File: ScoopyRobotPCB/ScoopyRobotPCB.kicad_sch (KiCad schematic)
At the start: 19 parts, among them J2 18V battery, J3 Raspberry_Pi_Header, M1 Gearmotor with encoder, M2 Gearmotor with encoder, M3 Roller gearmotor, M4 Tray gearmotor, SW1 Roller position, SW2 Tray down, SW3 Tray up, SW4 Pushbutton, SW5 Emergency stop, U1 D24V25F5 voltage regulator mo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

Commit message: Fixed typos in labels, connected properly now
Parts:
- renumbered J2 to J1, J3 to J2, M3 to M1, M4 to M2, M1 to M3, M2 to M4, U1 to Mod1, Mod1 to Mod2, Mod2 to Mod3, SW4 to SW1, SW5 to SW2, SW1 to SW3, SW2 to SW4, SW3 to SW5
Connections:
- net Roller position is gone; now on net Roll position: SW3.2 (B)
- net GND: now also J2.34 (Ground), J2.9 (Ground)
- net UI.SW: now also SW1.3 (B), SW1.4 (B)
- no-connect marks 7 -> 8
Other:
- moved on the sheet: SW1

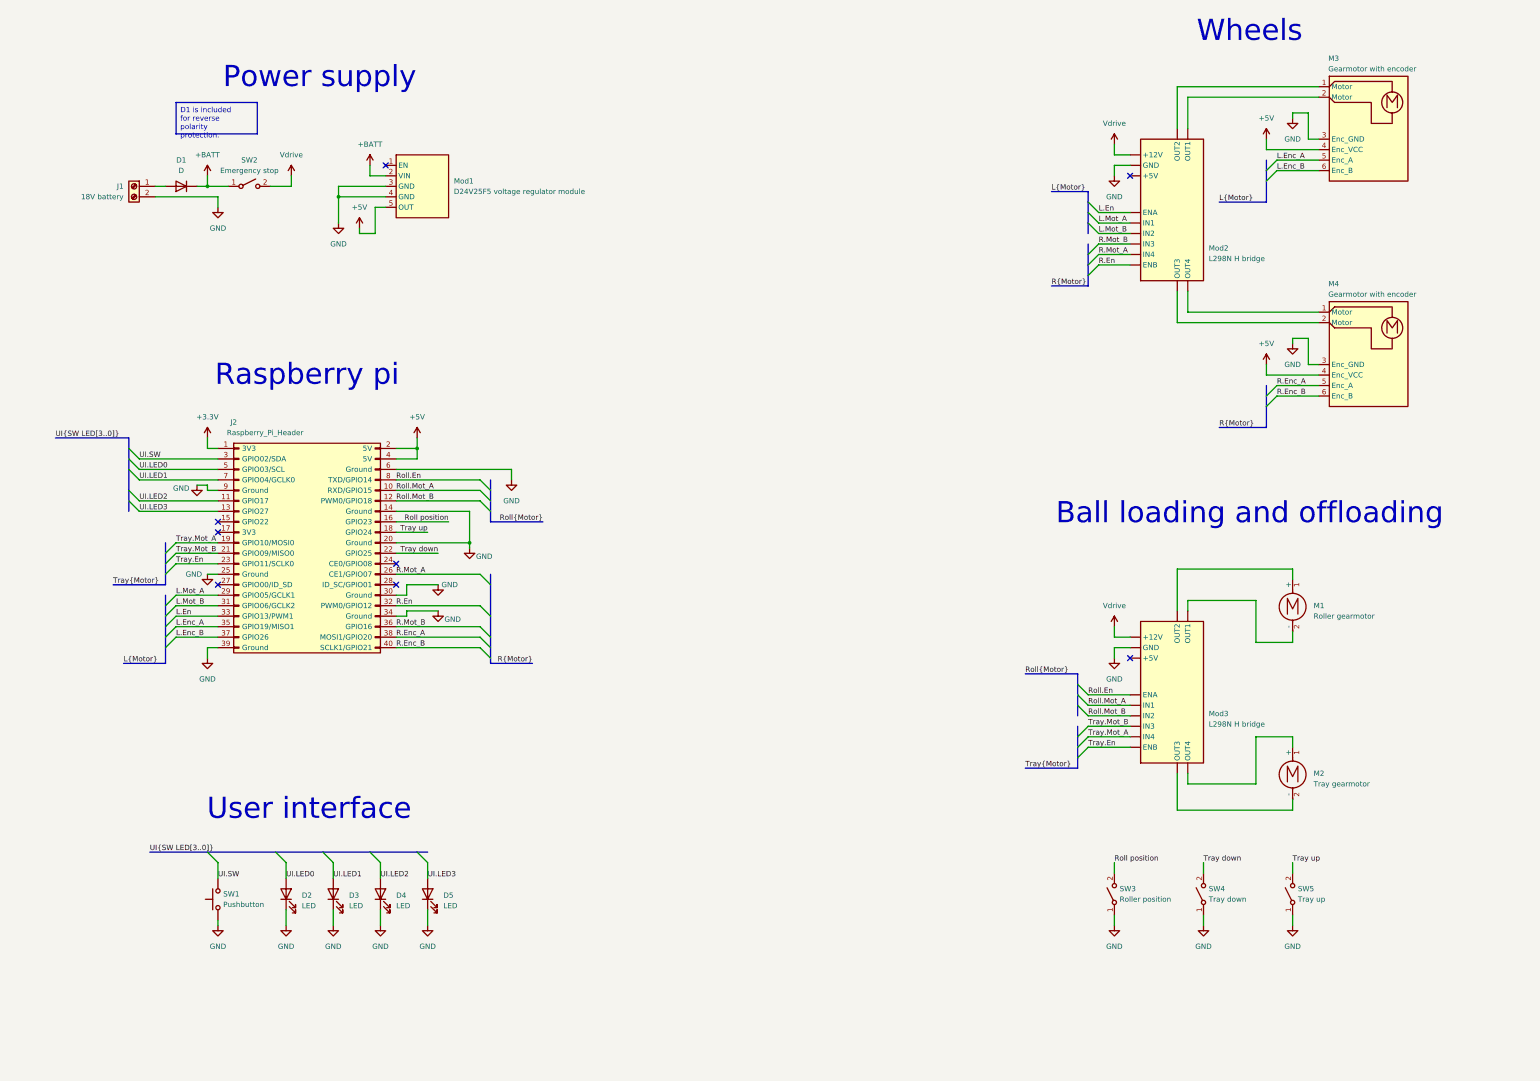
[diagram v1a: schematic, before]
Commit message: Fixing mistakes and typos in schematic, assigning footprints, starting veroboard layout
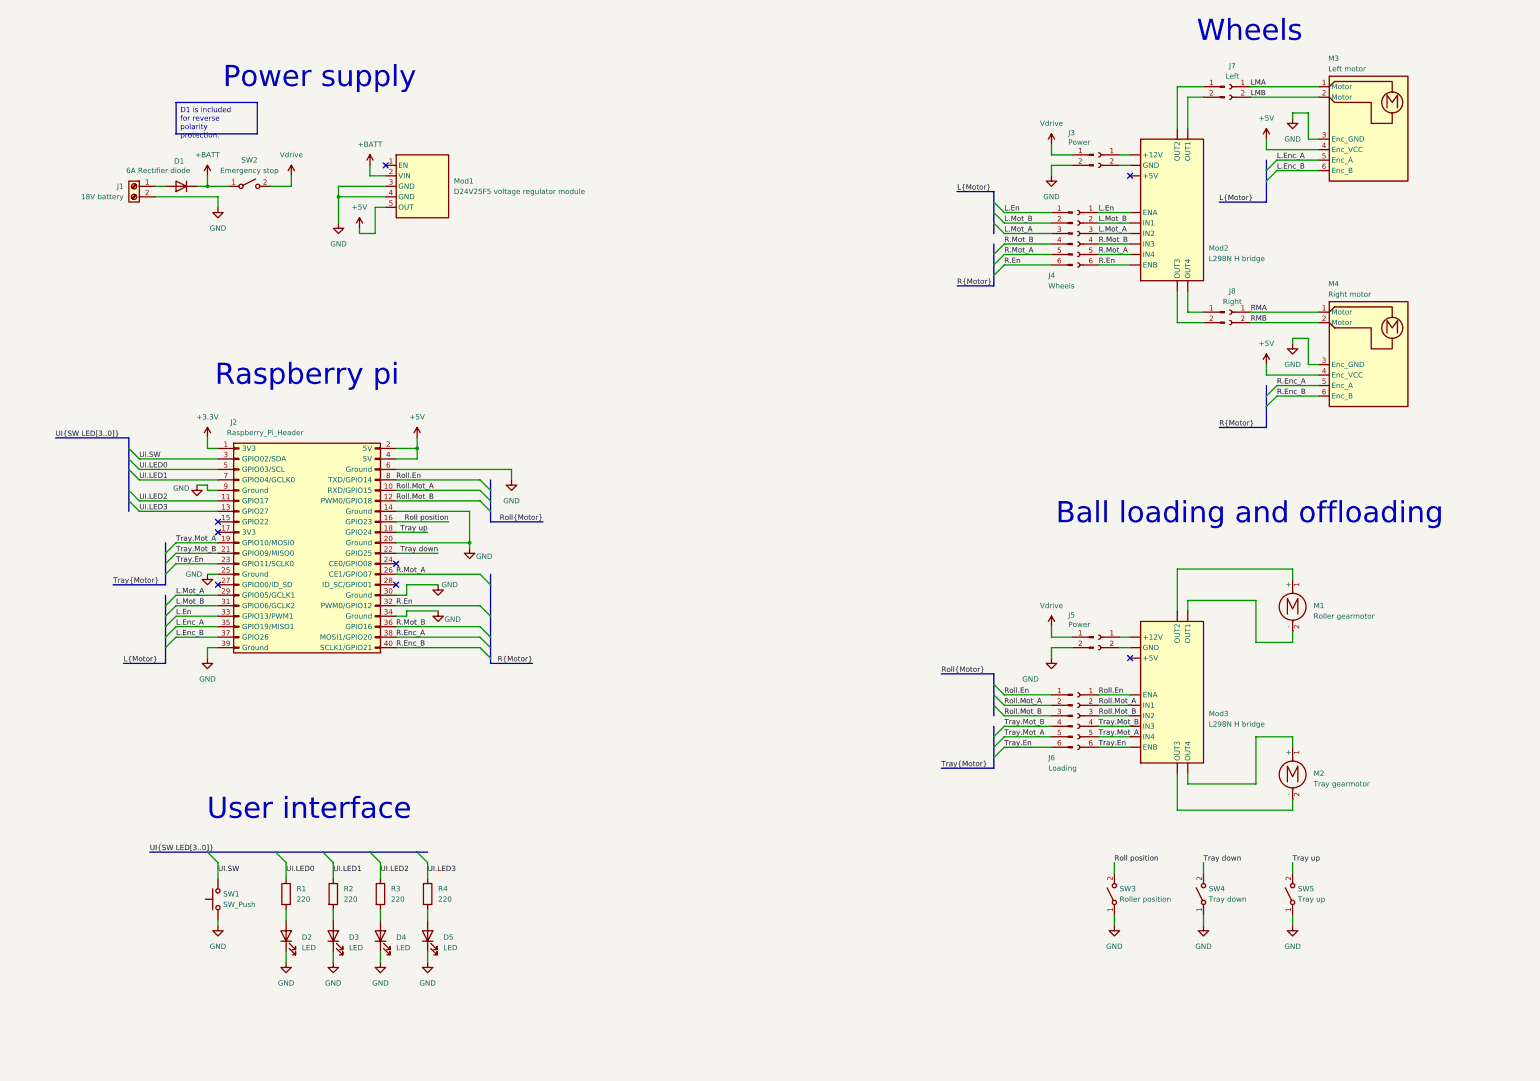
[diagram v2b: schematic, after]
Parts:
- removed SW1: Pushbutton, symbol Switch:SW_MEC_5G
- added #1, #3: Conn_01x02_Socket, symbol Connector:Conn_01x02_Socket
- added #2, #4: Wheels, symbol Connector:Conn_01x06_Socket
- added #5: Left motor, Connector_PinHeader_2.54mm:PinHeader_1x02_P2.54mm_Vertical, symbol Connector:Conn_01x02_Pin
- added #6: Right motor, Connector_PinHeader_2.54mm:PinHeader_1x02_P2.54mm_Vertical, symbol Connector:Conn_01x02_Pin
- added J3, J5: Power, Connector_PinHeader_2.54mm:PinHeader_1x02_P2.54mm_Vertical, symbol Connector:Conn_01x02_Pin
- added J4: Wheels, Connector_PinHeader_2.54mm:PinHeader_1x06_P2.54mm_Vertical, symbol Connector:Conn_01x06_Pin
- added J6: Loading, Connector_PinHeader_2.54mm:PinHeader_1x06_P2.54mm_Vertical, symbol Connector:Conn_01x06_Pin
- added J7: Left, Connector_PinSocket_2.54mm:PinSocket_1x02_P2.54mm_Vertical, symbol Connector:Conn_01x02_Socket
- added J8: Right, Connector_PinSocket_2.54mm:PinSocket_1x02_P2.54mm_Vertical, symbol Connector:Conn_01x02_Socket
- added R1, R2, R3, R4: 220, Resistor_THT:R_Axial_DIN0411_L9.9mm_D3.6mm_P12.70mm_Horizontal, symbol Device:R
- added SW1: SW_Push, Button_Switch_SMD:SW_SPST_Omron_B3FS-100xP, symbol Switch:SW_Push
- D1: value D -> 6A Rectifier diode; footprint (none) -> Diode_THT:D_DO-201_P15.24mm_Horizontal
- D2, D3, D4, D5: footprint (none) -> LED_THT:LED_D5.0mm
- J1, M1, M2, SW2: footprint (none) -> TerminalBlock_Phoenix:TerminalBlock_Phoenix_MKDS-1,5-2_1x02_P5.00mm_Horizontal
- M3: value Gearmotor with encoder -> Left motor; footprint (none) -> Connector_PinHeader_2.54mm:PinHeader_1x06_P2.54mm_Vertical
- M4: value Gearmotor with encoder -> Right motor; footprint (none) -> Connector_PinHeader_2.54mm:PinHeader_1x06_P2.54mm_Vertical
- Mod1: footprint (none) -> Connector_PinHeader_2.54mm:PinHeader_1x05_P2.54mm_Vertical
- SW3, SW4, SW5: footprint (none) -> Connector_PinSocket_2.54mm:PinSocket_1x02_P2.54mm_Vertical
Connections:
- net GND: now also J3.2 (Pin_2), J5.2 (Pin_2), SW1.1; no longer Mod2. (OUT4), Mod3. (OUT4)
- net L.En: now also #2.1 (Pin_1), J4.1 (Pin_1)
- net L.Mot_A: now also #2.3 (Pin_3), J4.3 (Pin_3)
- net L.Mot_B: now also #2.2 (Pin_2), J4.2 (Pin_2)
- net R.En: now also #2.6 (Pin_6), J4.6 (Pin_6)
- net R.Mot_A: now also #2.5 (Pin_5), J4.5 (Pin_5)
- net R.Mot_B: now also #2.4 (Pin_4), J4.4 (Pin_4)
- net Roll.En: now also #4.1 (Pin_1), J6.1 (Pin_1)
- net Roll.Mot_A: now also #4.2 (Pin_2), J6.2 (Pin_2)
- net Roll.Mot_B: now also #4.3 (Pin_3), J6.3 (Pin_3)
- net Tray.En: now also #4.6 (Pin_6), J6.6 (Pin_6)
- net Tray.Mot_A: now also #4.5 (Pin_5), J6.5 (Pin_5)
- net Tray.Mot_B: now also #4.4 (Pin_4), J6.4 (Pin_4)
- net UI.LED0: now also R1.1; no longer D2.2 (A)
- net UI.LED1: now also R2.1; no longer D3.2 (A)
- net UI.LED2: now also R3.1; no longer D4.2 (A)
- net UI.LED3: now also R4.1; no longer D5.2 (A)
- net UI.SW: now also SW1.2
- net Vdrive: now also J3.1 (Pin_1), J5.1 (Pin_1); no longer Mod2. (OUT4), Mod3. (OUT4)
- net LMA: now reaches M3.1 (Motor)
- net LMA: now also J7.1 (Pin_1); no longer Mod2. (OUT4)
- net LMB: now reaches M3.2 (Motor)
- net LMB: now also J7.2 (Pin_2); no longer Mod2. (OUT4)
- net RMA: now reaches M4.1 (Motor)
- net RMA: now also J8.1 (Pin_1); no longer Mod2. (OUT4)
- net RMB: now reaches M4.2 (Motor)
- net RMB: now also J8.2 (Pin_2); no longer Mod2. (OUT4)
- new net: D2.2 (A), R1.2
- new net: #1.1 (Pin_1), Mod2. (OUT4)
- new net: #1.2 (Pin_2), Mod2. (OUT4)
- new net: #3.1 (Pin_1), Mod3. (OUT4)
- new net: #3.2 (Pin_2), Mod3. (OUT4)
- new net: D5.2 (A), R4.2
- new net: #6.1 (Pin_1), Mod2. (OUT4)
- new net: #6.2 (Pin_2), Mod2. (OUT4)
- new net: #5.1 (Pin_1), Mod2. (OUT4)
- new net: #5.2 (Pin_2), Mod2. (OUT4)
- new net: D3.2 (A), R2.2
- new net: D4.2 (A), R3.2
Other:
- moved on the sheet: D2, D3, D4, D5

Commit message: Added voltage dividers for encoder, need to update layout to make way for ethernet header
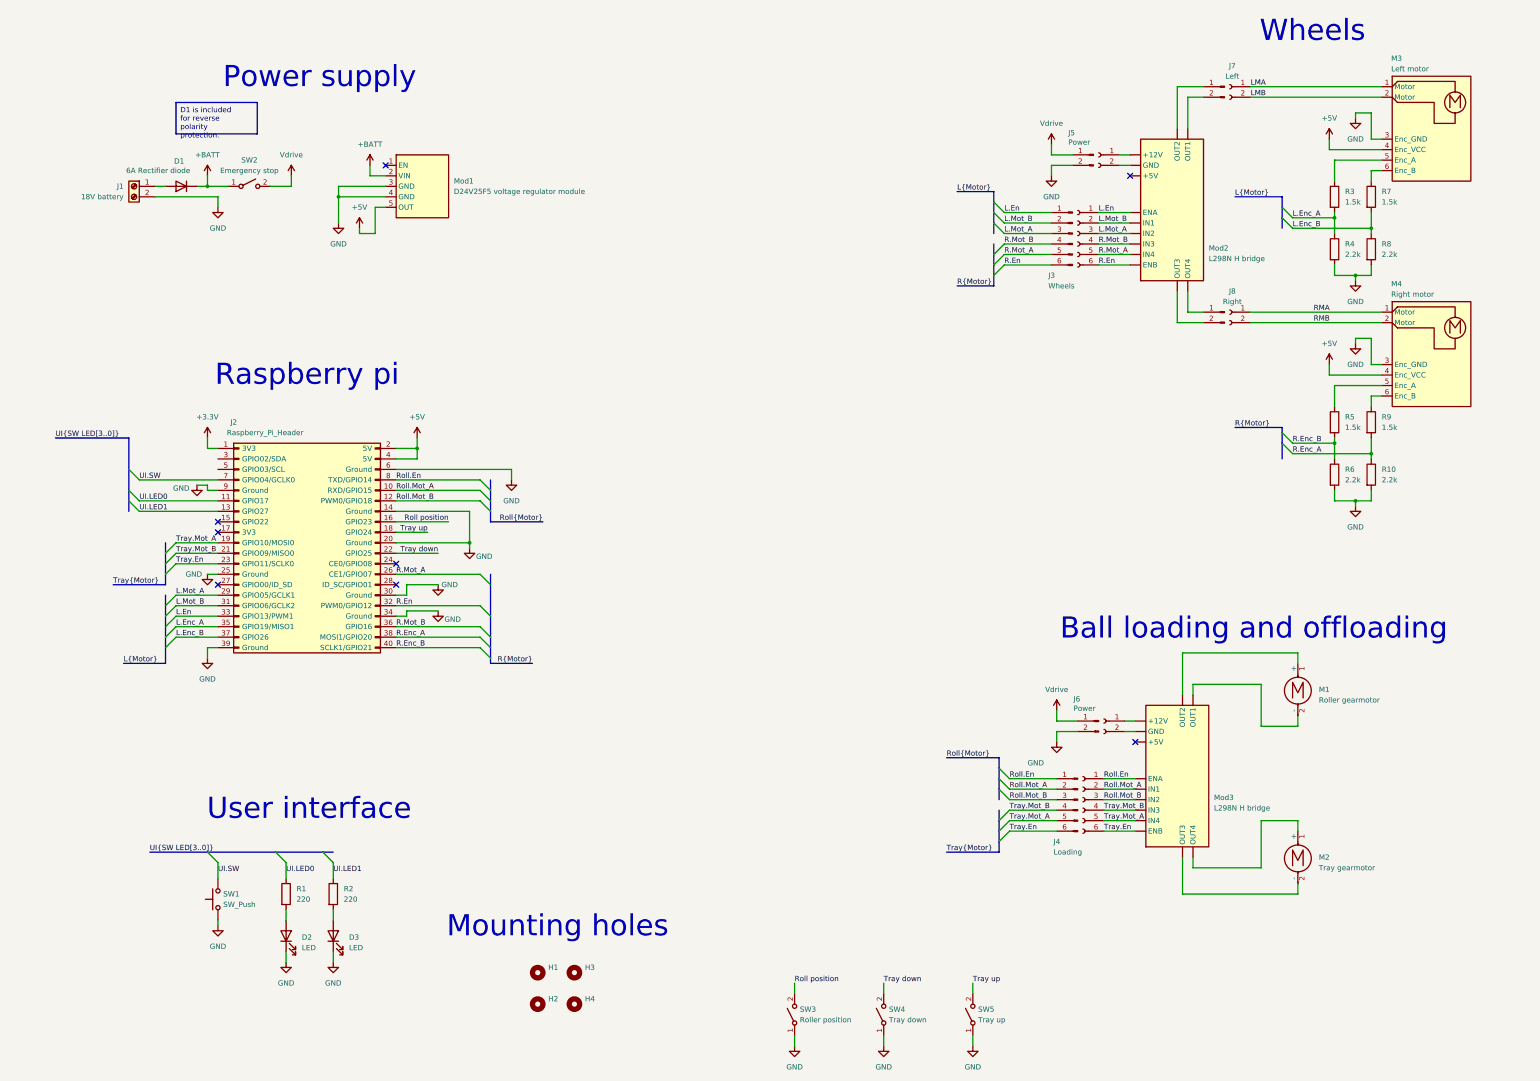
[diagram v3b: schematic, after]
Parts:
- removed D4, D5: LED, LED_THT:LED_D5.0mm, symbol Device:LED
- added H1, H2, H3, H4: MountingHole, MountingHole:MountingHole_3.2mm_M3, symbol Mechanical:MountingHole
- added R10, R8: 2.2k, Resistor_THT:R_Axial_DIN0411_L9.9mm_D3.6mm_P5.08mm_Vertical, symbol Device:R
- added R5, R7, R9: 1.5k, Resistor_THT:R_Axial_DIN0411_L9.9mm_D3.6mm_P7.62mm_Vertical, symbol Device:R
- added R6: 2.2k, Resistor_THT:R_Axial_DIN0309_L9.0mm_D3.2mm_P2.54mm_Vertical, symbol Device:R
- J2: footprint Connector_PinHeader_2.54mm:PinHeader_2x20_P2.54mm_Vertical -> Connector_PinSocket_2.54mm:PinSocket_2x20_P2.54mm_Vertical
- J7, J8, SW3, SW4, SW5: footprint Connector_PinSocket_2.54mm:PinSocket_1x02_P2.54mm_Vertical -> Connector_PinHeader_2.54mm:PinHeader_1x02_P2.54mm_Vertical
- R3: value 220 -> 1.5k; footprint Resistor_THT:R_Axial_DIN0411_L9.9mm_D3.6mm_P12.70mm_Horizontal -> Resistor_THT:R_Axial_DIN0411_L9.9mm_D3.6mm_P7.62mm_Vertical
- R4: value 220 -> 2.2k; footprint Resistor_THT:R_Axial_DIN0411_L9.9mm_D3.6mm_P12.70mm_Horizontal -> Resistor_THT:R_Axial_DIN0207_L6.3mm_D2.5mm_P2.54mm_Vertical
- SW1: footprint Button_Switch_SMD:SW_SPST_Omron_B3FS-100xP -> Button_Switch_THT:SW_PUSH_6mm
- renumbered #2 to #1, #4 to #2, #1 to #3, #3 to #4, J4 to J3, J6 to J4, J3 to J5, J5 to J6
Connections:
- net GND: now also R4.2, R10.2, R6.2, R8.2
- net L.Enc_A: now also R3.2, R4.1; no longer M3.5 (Enc_A)
- net L.Enc_B: now also R7.2, R8.1; no longer M3.6 (Enc_B)
- net R.Enc_A: now also R10.1, R9.2; no longer M4.5 (Enc_A)
- net R.Enc_B: now also R5.2, R6.1; no longer M4.6 (Enc_B)
- net UI.LED0: now also J2.11 (GPIO17); no longer J2.5 (GPIO03/SCL)
- net UI.LED1: now also J2.13 (GPIO27); no longer J2.7 (GPIO04/GCLK0)
- net UI.SW: now also J2.7 (GPIO04/GCLK0); no longer J2.3 (GPIO02/SDA)
- net UI.LED2: no longer names the net of R3.1
- net UI.LED2: now also M3.5 (Enc_A); no longer J2.11 (GPIO17)
- removed net UI.LED3: J2.13 (GPIO27), R4.1
- new net: M3.6 (Enc_B), R7.1
- new net: M4.5 (Enc_A), R5.1
- new net: M4.6 (Enc_B), R9.1
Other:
- note added: "Mounting holes"
- moved on the sheet: J4, J6, M1, M2, M3, M4, Mod3, SW3, SW4, SW5

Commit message: Added missing track on PCB
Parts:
- R10: value 2.2k -> 1k
- R3, R7: value 1.5k -> 2.2k
- R5, R9: value 1.5k -> 1k
- R6: value 2.2k -> 1.k
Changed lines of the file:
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@@
 			)
 		)
-		(property "Value" "1.5k"
+		(property "Value" "2.2k"
 			(at 369.57 66.0399 0)
 			(effects
@@
 			)
 		)
-		(property "Value" "2.2k"
+		(property "Value" "1.k"
 			(at 360.68 133.3499 0)
 			(effects
@@
 			)
 		)
-		(property "Value" "1.5k"
+		(property "Value" "2.2k"
 			(at 360.68 66.0399 0)
 			(effects
@@
 	)
 	(symbol
-		(lib_name "Custom:L298N_Motor_Driver_H_Bridge")
 		(lib_id "Custom:L298N_Motor_Driver_H_Bridge")
 		(at 312.42 222.25 90)
@@
 			)
 		)
-		(property "Value" "1.5k"
+		(property "Value" "1k"
 			(at 369.57 120.6499 0)
 			(effects
@@
 	)
 	(symbol
-		(lib_name "Custom:L298N_Motor_Driver_H_Bridge")
 		(lib_id "Custom:L298N_Motor_Driver_H_Bridge")
 		(at 311.15 85.09 90)
@@
 			)
 		)
-		(property "Value" "2.2k"
+		(property "Value" "1k"
 			(at 369.57 133.3499 0)
 			(effects
@@
 			)
 		)
-		(property "Value" "1.5k"
+		(property "Value" "1k"
 			(at 360.68 120.6499 0)
 			(effects

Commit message: Started to update PCB
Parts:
- removed #2: Wheels, symbol Connector:Conn_01x06_Socket
- removed #4: Conn_01x02_Socket, symbol Connector:Conn_01x02_Socket
- removed J4: Loading, Connector_PinHeader_2.54mm:PinHeader_1x06_P2.54mm_Vertical, symbol Connector:Conn_01x06_Pin
- removed J6: Power, Connector_PinHeader_2.54mm:PinHeader_1x02_P2.54mm_Vertical, symbol Connector:Conn_01x02_Pin
- removed M2: Tray gearmotor, TerminalBlock_Phoenix:TerminalBlock_Phoenix_MKDS-1,5-2_1x02_P5.00mm_Horizontal, symbol Motor:Motor_DC
- removed Mod3: L298N H bridge, symbol Custom:L298N_Motor_Driver_H_Bridge
- removed SW4: Tray down, Connector_PinHeader_2.54mm:PinHeader_1x02_P2.54mm_Vertical, symbol Switch:SW_SPST
- removed SW5: Tray up, Connector_PinHeader_2.54mm:PinHeader_1x02_P2.54mm_Vertical, symbol Switch:SW_SPST
- added D4: 1N4004, Diode_THT:D_DO-41_SOD81_P10.16mm_Horizontal, symbol Diode:1N4004
- added Q1: Q_NPN_Darlington_BCE, symbol Device:Q_NPN_Darlington_BCE
- added R11: 390, symbol Device:R
- M1: value Roller gearmotor -> Chain gearmotor
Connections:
- net GND: now also Q1.3 (E)
- net L.Mot_A: no longer J2.29 (GPIO05/GCLK1)
- net Vdrive: now also M1.1 (+), D4.1 (K)
- net at M1.2 (-): now also D4.2 (A), Q1.2 (C)
- net Roll position renamed Chain position
- net Roll.En: no longer names the net of J2.8 (TXD/GPIO14)
- net Roll.Mot_A: no longer names the net of J2.10 (RXD/GPIO15)
- net Roll.Mot_B: no longer names the net of J2.12 (PWM0/GPIO18)
- net Tray down: no longer names the net of J2.22 (GPIO25)
- net Tray up renamed Chain motor
- net Chain motor: now also R11.1
- net Tray.En: no longer names the net of J2.23 (GPIO11/SCLK0)
- net Tray.Mot_A: no longer names the net of J2.19 (GPIO10/MOSI0)
- net Tray.Mot_B: no longer names the net of J2.21 (GPIO09/MISO0)
- new net: Q1.1 (B), R11.2
- no-connect marks 8 -> 7
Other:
- moved on the sheet: M1, SW3

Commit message: Schematic finished
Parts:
- added J3: Left colour sensor, Connector_PinHeader_2.54mm:PinHeader_1x04_P2.54mm_Vertical, symbol Connector:Conn_01x04_Pin
- added J4: Right colour sensor, Connector_PinHeader_2.54mm:PinHeader_1x04_P2.54mm_Vertical, symbol Connector:Conn_01x04_Pin
- Q1: footprint (none) -> Package_TO_SOT_THT:TO-220-3_Vertical
- R10: renamed from R9; value 1k -> 10k
- R11: renamed from R10; value 1k -> 10k
- R3: renamed from R11; footprint (none) -> Resistor_THT:R_Axial_DIN0411_L9.9mm_D3.6mm_P7.62mm_Vertical
- R4: renamed from R3; value 2.2k -> 10k
- R5: renamed from R4; value 2.2k -> 10k
- R6: renamed from R5; value 1k -> 10k
- R7: renamed from R6; value 1.k -> 10k
- R8: renamed from R7; value 2.2k -> 10k
- R9: renamed from R8; value 2.2k -> 10k
- renumbered #3 to #2, #5 to #3, #6 to #4, J3 to J5, J5 to J6, M3 to M2, M4 to M3
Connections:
- net +3.3V: now also J3.4 (Pin_4), J4.4 (Pin_4)
- net Chain motor: now also J2.10 (RXD/GPIO15); no longer J2.18 (GPIO24)
- net Chain position: now also J2.22 (GPIO25); no longer J2.16 (GPIO23)
- net GND: now also J3.3 (Pin_3), J4.3 (Pin_3)
- net LC.SCL: now reaches J2.3 (GPIO02/SDA)
- net LC.SCL: now also J3.2 (Pin_2)
- net LC.SDA: now reaches J2.5 (GPIO03/SCL)
- net LC.SDA: now also J3.1 (Pin_1)
- new net RC.SCL: J2.18 (GPIO24), J4.2 (Pin_2)
- new net RC.SDA: J2.16 (GPIO23), J4.1 (Pin_1)
- no-connect marks 7 -> 12
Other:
- note added: "Colour sensors"

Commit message: PCB layout updated to currentish
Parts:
- D4: footprint Diode_THT:D_DO-41_SOD81_P10.16mm_Horizontal -> Diode_THT:D_DO-41_SOD81_P2.54mm_Vertical_KathodeUp
- M1: footprint TerminalBlock_Phoenix:TerminalBlock_Phoenix_MKDS-1,5-2_1x02_P5.00mm_Horizontal -> Connector_PinHeader_2.54mm:PinHeader_1x02_P2.54mm_Vertical
- R3: footprint Resistor_THT:R_Axial_DIN0411_L9.9mm_D3.6mm_P7.62mm_Vertical -> Resistor_THT:R_Axial_DIN0411_L9.9mm_D3.6mm_P5.08mm_Vertical
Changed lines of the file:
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@@
 			)
 		)
-		(property "Footprint" "Diode_THT:D_DO-41_SOD81_P10.16mm_Horizontal"
+		(property "Footprint" "Diode_THT:D_DO-41_SOD81_P2.54mm_Vertical_KathodeUp"
 			(at 330.835 203.2 0)
 			(effects
@@
 		(exclude_from_sim no)
 		(in_bom yes)
-		(on_board no)
+		(on_board yes)
 		(dnp no)
 		(fields_autoplaced yes)
@@
 			)
 		)
-		(property "Footprint" "TerminalBlock_Phoenix:TerminalBlock_Phoenix_MKDS-1,5-2_1x02_P5.00mm_Horizontal"
+		(property "Footprint" "Connector_PinHeader_2.54mm:PinHeader_1x02_P2.54mm_Vertical"
 			(at 351.79 206.756 0)
 			(effects
@@
 			)
 		)
-		(property "Footprint" "Resistor_THT:R_Axial_DIN0411_L9.9mm_D3.6mm_P7.62mm_Vertical"
+		(property "Footprint" "Resistor_THT:R_Axial_DIN0411_L9.9mm_D3.6mm_P5.08mm_Vertical"
 			(at 337.82 227.838 90)
 			(effects
